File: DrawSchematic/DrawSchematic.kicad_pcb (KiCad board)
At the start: 2 copper layers, 18 x 21 mm, 8 parts, among them J1 POWER INPUT, U1 LM555xN

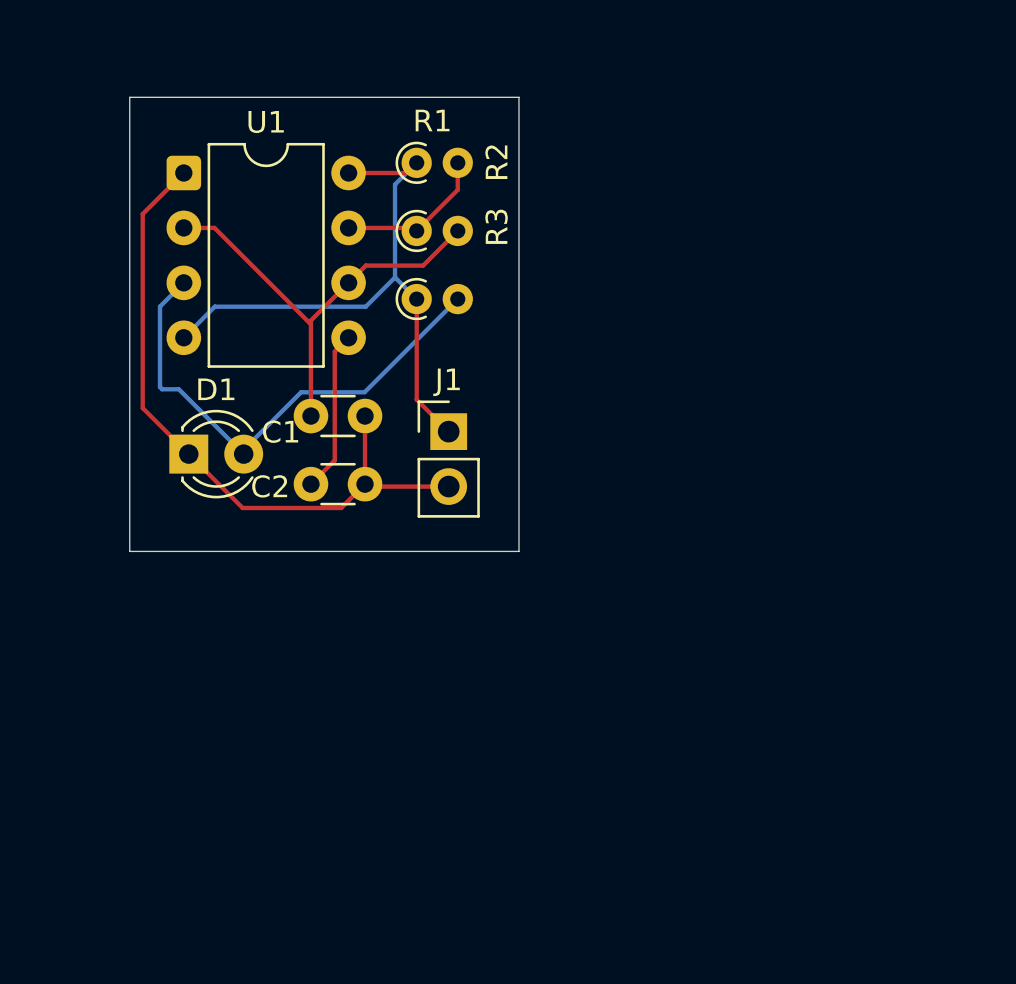
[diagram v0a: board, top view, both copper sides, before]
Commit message: added logo library
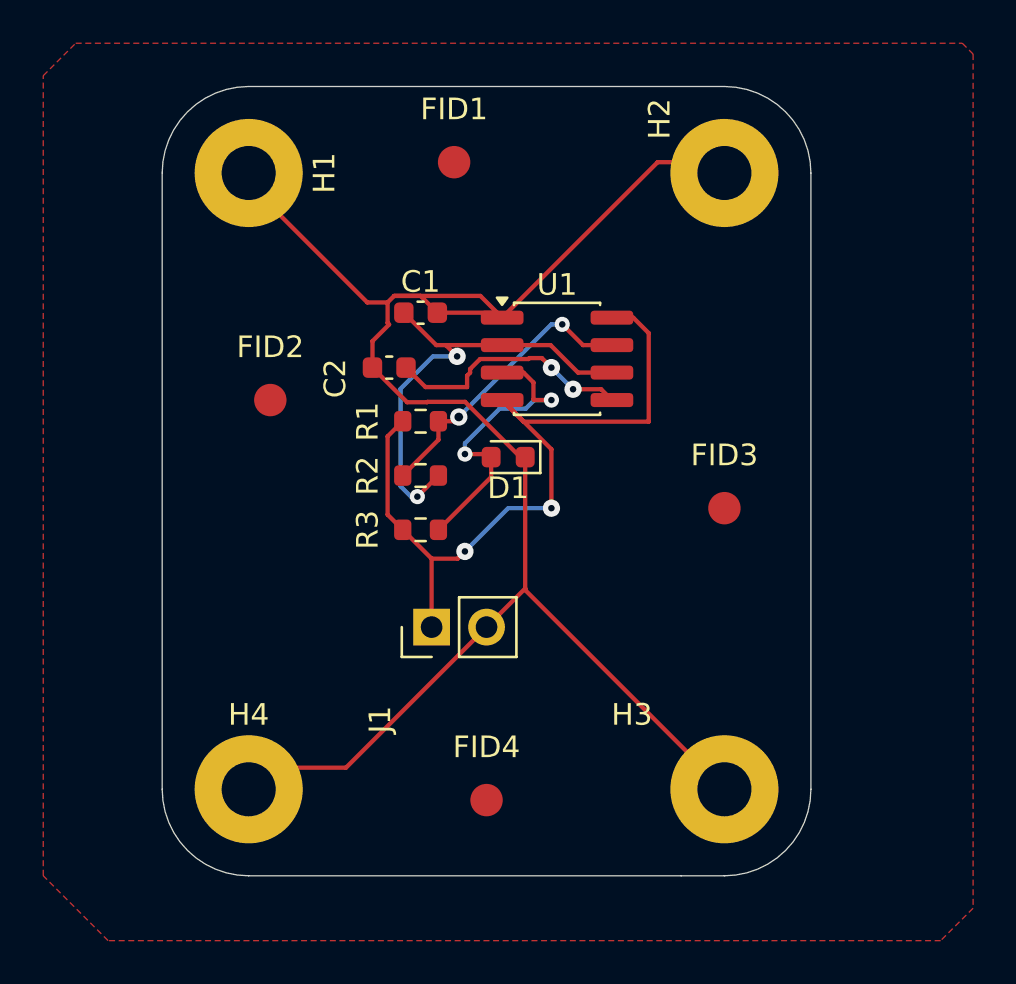
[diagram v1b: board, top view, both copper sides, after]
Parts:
- added FID1: Fiducial, Fiducial:Fiducial_1.5mm_Mask3mm, F.Cu at (144.0, 83.0)
- added FID2: Fiducial, Fiducial:Fiducial_1.5mm_Mask3mm, F.Cu at (135.5, 94.0)
- added FID3: Fiducial, Fiducial:Fiducial_1.5mm_Mask3mm, F.Cu at (156.5, 99.0)
- added FID4: Fiducial, Fiducial:Fiducial_1.5mm_Mask3mm, F.Cu at (145.5, 112.5)
- added H1: MountingHole_Pad, MountingHole:MountingHole_2.5mm_Pad, F.Cu at (134.5, 83.5)
- added H2: MountingHole_Pad, MountingHole:MountingHole_2.5mm_Pad, F.Cu at (156.5, 83.5)
- added H3: MountingHole_Pad, MountingHole:MountingHole_2.5mm_Pad, F.Cu at (156.5, 112.0)
- added H4: MountingHole_Pad, MountingHole:MountingHole_2.5mm_Pad, F.Cu at (134.5, 112.0)
- C1, C2: footprint Capacitor_THT:C_Disc_D3.0mm_W1.6mm_P2.50mm -> Capacitor_SMD:C_0603_1608Metric
- D1: footprint LED_THT:LED_D3.0mm -> LED_SMD:LED_0603_1608Metric
- R1, R2, R3: footprint Resistor_THT:R_Axial_DIN0204_L3.6mm_D1.6mm_P1.90mm_Vertical -> Resistor_SMD:R_0603_1608Metric
- U1: footprint Package_DIP:DIP-8_W7.62mm -> Package_SO:SOP-8_3.76x4.96mm_P1.27mm
- moved U1 19.3 mm to (148.8, 92.1)
- moved D1 14.8 mm to (146.5, 96.6), turned to 180 degrees
- moved R1 12.0 mm to (142.4, 95.0)
- moved R2 11.3 mm to (142.4, 97.5)
- moved R3 10.7 mm to (142.4, 100.0)
- moved J1 9.07 mm to (143.0, 104.5), turned to 90 degrees
- moved C1 6.97 mm to (142.4, 90.0)
- moved C2 6.49 mm to (141.0, 92.5), turned to 180 degrees
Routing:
- net GND: track 31.4 -> 80.0 mm
- net Net-(D1-A): track 23.4 -> 14.2 mm, vias 0 -> 2
- net VCC: track 28.1 -> 36.4 mm, vias 0 -> 2
- net DIS: track 7.14 -> 13.5 mm, vias 0 -> 2
- net Net-(U1-CV): track 7.49 -> 11.9 mm, vias 0 -> 2
- net TRG: track 20.7 -> 21.6 mm, vias 0 -> 2
- added copper zone on F.Cu, net GND
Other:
- board size 18 x 21 mm -> 30 x 36.5 mm
